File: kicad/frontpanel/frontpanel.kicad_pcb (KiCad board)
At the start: 2 copper layers, 45.7 x 128.5 mm, 0 parts

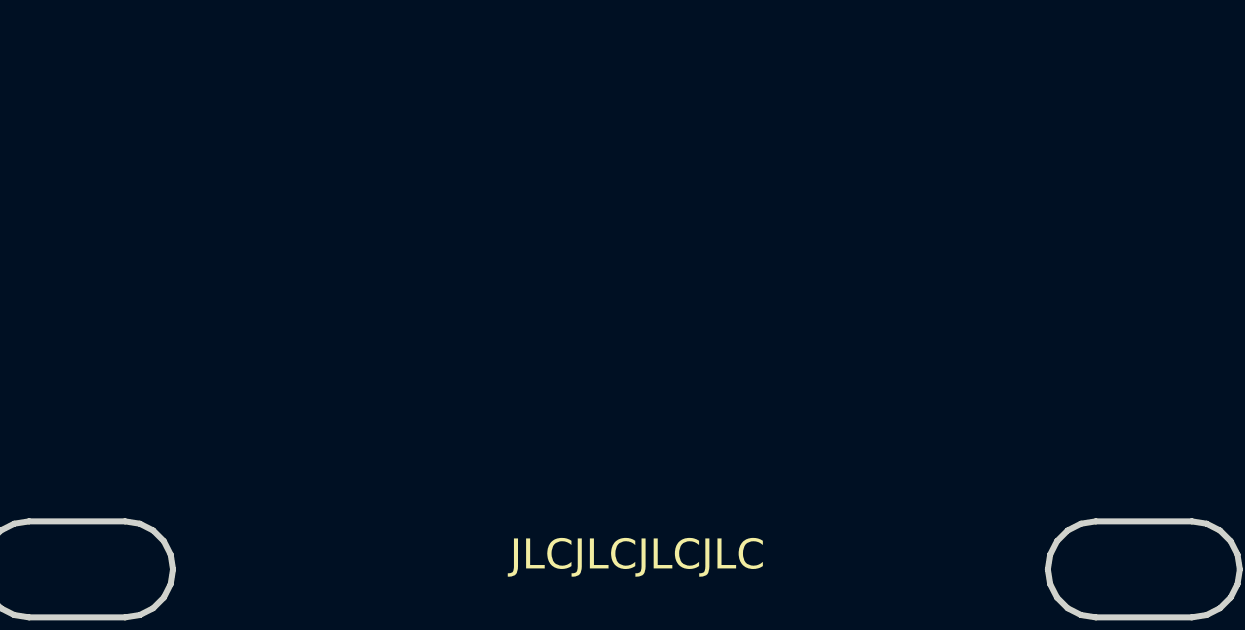
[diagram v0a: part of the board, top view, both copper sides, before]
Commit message: Silkscreen and text updates.
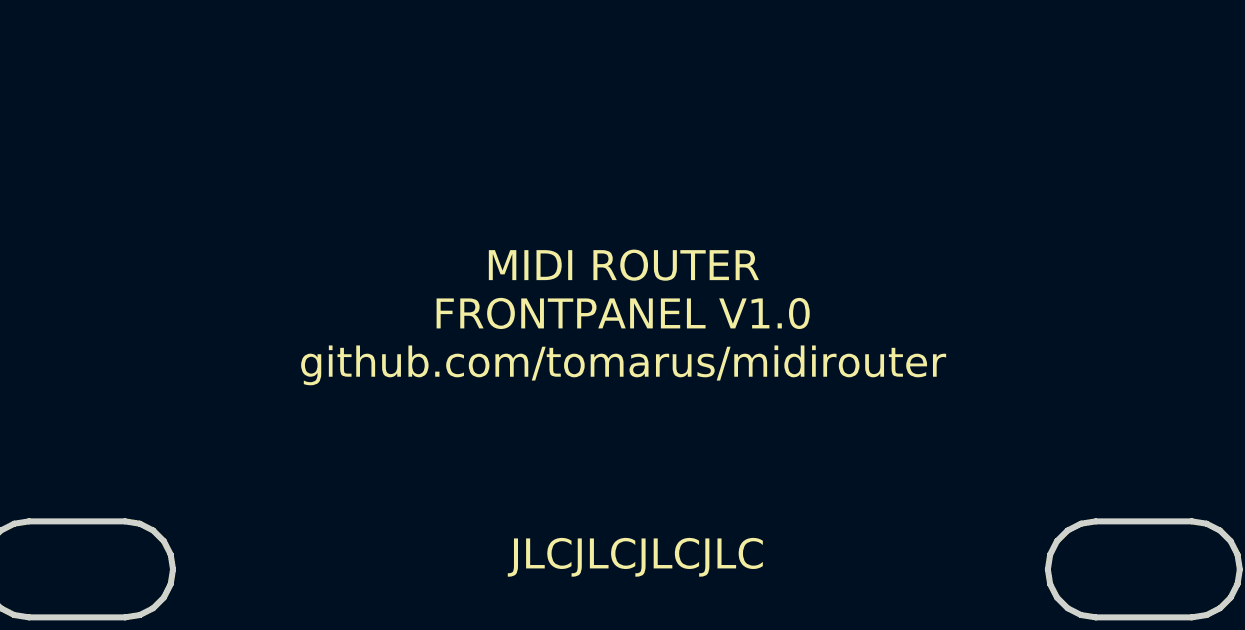
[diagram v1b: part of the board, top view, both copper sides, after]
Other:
- board text added: "BY TOMARUS"
- board text added: "MIDI ROUTER FRONTPANEL V1.0 github.com/tomarus/midirouter"
- board text removed: "TOMARUS"
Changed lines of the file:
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@@
   (general
     (thickness 1.6)
-    (drawings 894)
+    (drawings 895)
     (tracks 0)
     (zones 0)
@@
     (uvia_drill 0.1)
   )
+  (gr_text "MIDI ROUTER\nFRONTPANEL V1.0\ngithub.com/tomarus/midirouter" (at 122 142) (layer F.SilkS)
+    (effects (font (size 1 1) (thickness 0.15)))
+  )
   (gr_text IN (at 133.5 89.5) (layer B.SilkS)
     (effects (font (size 1.5 1.5) (thickness 0.3)) (justify mirror))
@@
     (effects (font (size 1.5 1.5) (thickness 0.3)) (justify mirror))
   )
-  (gr_text "MIDI ROUTER" (at 122.5 145) (layer B.SilkS)
-    (effects (font (size 3.5 3.5) (thickness 0.5)) (justify mirror))
+  (gr_text "MIDI ROUTER" (at 122.5 147) (layer B.SilkS)
+    (effects (font (size 2 2) (thickness 0.2)) (justify mirror))
   )
   (gr_text IN (at 133.5 132.5) (layer B.SilkS)
@@
     (effects (font (size 1.5 1.5) (thickness 0.3)) (justify mirror))
   )
-  (gr_text TOMARUS (at 122.5 150.5) (layer B.SilkS)
-    (effects (font (size 3.5 3.5) (thickness 0.5)) (justify mirror))
+  (gr_text "BY TOMARUS" (at 122.5 150.5) (layer B.SilkS)
+    (effects (font (size 2 2) (thickness 0.2)) (justify mirror))
   )
   (gr_text JLCJLCJLCJLC (at 122.5 150) (layer F.SilkS)
     (effects (font (size 1 1) (thickness 0.15)))
   )
-  (gr_text "MIDI x4" (at 122.5 35) (layer B.SilkS)
+  (gr_text "MIDI x4" (at 122.5 38) (layer B.SilkS)
     (effects (font (size 6 6) (thickness 1)) (justify mirror))
   )

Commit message: Revision A PCBs.
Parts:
- added REF**: MountingHole_3.2mm_M3, MountingHole:MountingHole_3.2mm_M3, F.Cu at (33.9, 167.8)
- added REF**: MountingHole_3.2mm_M3, MountingHole:MountingHole_3.2mm_M3, F.Cu at (11.8, 167.8)
- added REF**: MountingHole_3.2mm_M3, MountingHole:MountingHole_3.2mm_M3, F.Cu at (11.8, 123.8)
- added REF**: MountingHole_3.2mm_M3, MountingHole:MountingHole_3.2mm_M3, F.Cu at (33.9, 123.8)
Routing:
- added copper zone on F.Cu, net (none)
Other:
- outline, holes or cut-outs redrawn
- board text added: "MIDI Router Frontpanel github.com/tomarus/midirouter"
- board text added: "TOMARUS"
- board text removed: "BY TOMARUS"
- board text removed: "MIDI ROUTER"
- board text removed: "MIDI ROUTER FRONTPANEL V1.0 github.com/tomarus/midirouter"
